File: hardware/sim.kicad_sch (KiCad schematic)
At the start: 11 parts, among them J12 Conn_01x06, J13 SIM_Card

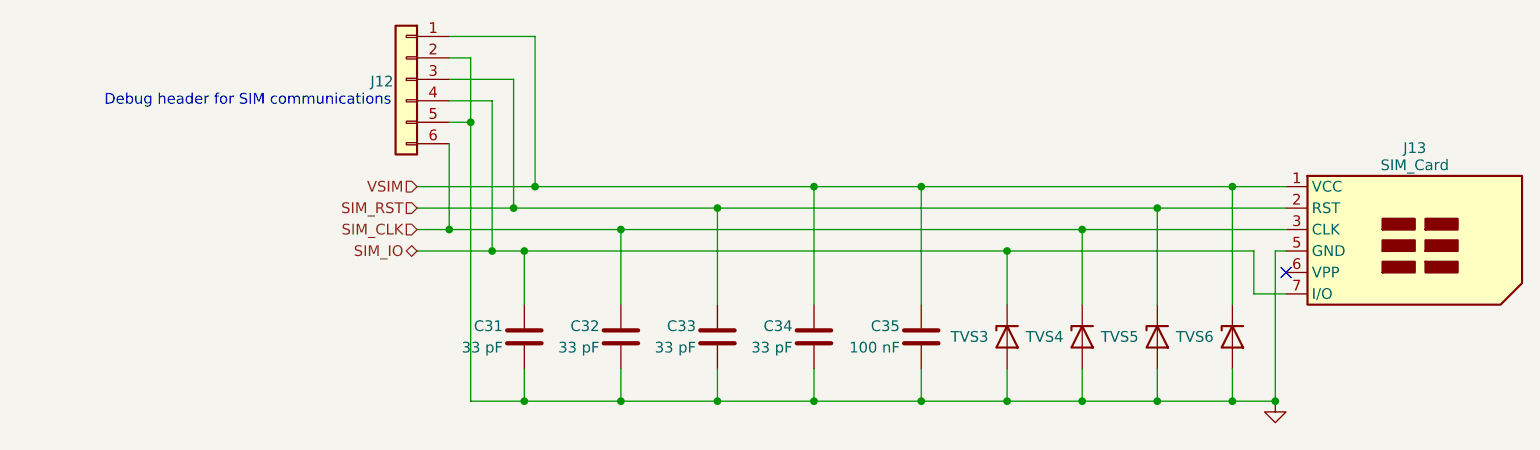
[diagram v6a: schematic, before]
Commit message: HW: Cleanup schematic
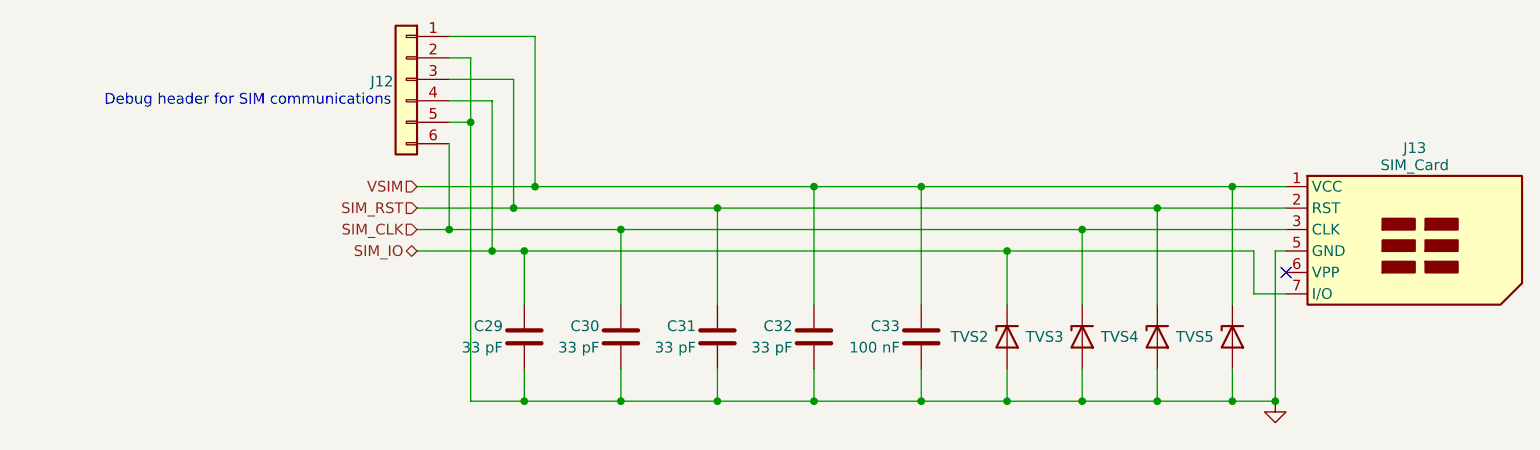
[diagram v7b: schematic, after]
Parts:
- renumbered C31 to C29, C32 to C30, C33 to C31, C34 to C32, C35 to C33, TVS3 to TVS2, TVS4 to TVS3, TVS5 to TVS4, TVS6 to TVS5
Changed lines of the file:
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@@
 		(on_board yes)
 		(dnp no)
-		(property "Reference" "C35"
+		(property "Reference" "C33"
 			(at 143.51 135.89 0)
 			(effects
@@
 			(project "iida_devkit"
 				(path "/b12a6e25-97fb-4aba-bc96-af8db389bb9a/33580d9f-a609-4568-baaf-9a29cf2dabcd"
-					(reference "C35")
+					(reference "C33")
 					(unit 1)
 				)
@@
 		(on_board yes)
 		(dnp no)
-		(property "Reference" "TVS4"
+		(property "Reference" "TVS3"
 			(at 160.655 137.16 90)
 			(effects
@@
 			(project "iida_devkit"
 				(path "/b12a6e25-97fb-4aba-bc96-af8db389bb9a/33580d9f-a609-4568-baaf-9a29cf2dabcd"
-					(reference "TVS4")
+					(reference "TVS3")
 					(unit 1)
 				)
@@
 		(on_board yes)
 		(dnp no)
-		(property "Reference" "C32"
+		(property "Reference" "C30"
 			(at 107.95 135.89 0)
 			(effects
@@
 			(project "iida_devkit"
 				(path "/b12a6e25-97fb-4aba-bc96-af8db389bb9a/33580d9f-a609-4568-baaf-9a29cf2dabcd"
-					(reference "C32")
+					(reference "C30")
 					(unit 1)
 				)
@@
 		(on_board yes)
 		(dnp no)
-		(property "Reference" "C31"
+		(property "Reference" "C29"
 			(at 96.52 135.89 0)
 			(effects
@@
 			(project "iida_devkit"
 				(path "/b12a6e25-97fb-4aba-bc96-af8db389bb9a/33580d9f-a609-4568-baaf-9a29cf2dabcd"
-					(reference "C31")
+					(reference "C29")
 					(unit 1)
 				)
@@
 		(on_board yes)
 		(dnp no)
-		(property "Reference" "TVS6"
+		(property "Reference" "TVS5"
 			(at 178.435 137.16 90)
 			(effects
@@
 			(project "iida_devkit"
 				(path "/b12a6e25-97fb-4aba-bc96-af8db389bb9a/33580d9f-a609-4568-baaf-9a29cf2dabcd"
-					(reference "TVS6")
+					(reference "TVS5")
 					(unit 1)
 				)
@@
 		(on_board yes)
 		(dnp no)
-		(property "Reference" "TVS3"
+		(property "Reference" "TVS2"
 			(at 151.765 137.16 90)
 			(effects
@@
 			(project "iida_devkit"
 				(path "/b12a6e25-97fb-4aba-bc96-af8db389bb9a/33580d9f-a609-4568-baaf-9a29cf2dabcd"
-					(reference "TVS3")
+					(reference "TVS2")
 					(unit 1)
 				)
@@
 		(on_board yes)
 		(dnp no)
-		(property "Reference" "C33"
+		(property "Reference" "C31"
 			(at 119.38 135.89 0)
 			(effects
@@
 			(project "iida_devkit"
 				(path "/b12a6e25-97fb-4aba-bc96-af8db389bb9a/33580d9f-a609-4568-baaf-9a29cf2dabcd"
-					(reference "C33")
+					(reference "C31")
 					(unit 1)
 				)
@@
 		(on_board yes)
 		(dnp no)
-		(property "Reference" "TVS5"
+		(property "Reference" "TVS4"
 			(at 169.545 137.16 90)
 			(effects
@@
 			(project "iida_devkit"
 				(path "/b12a6e25-97fb-4aba-bc96-af8db389bb9a/33580d9f-a609-4568-baaf-9a29cf2dabcd"
-					(reference "TVS5")
+					(reference "TVS4")
 					(unit 1)
 				)
@@
 		(dnp no)
 		(fields_autoplaced yes)
-		(property "Reference" "#PWR026"
+		(property "Reference" "#PWR024"
 			(at 187.96 151.13 0)
 			(effects
@@
 			(project "iida_devkit"
 				(path "/b12a6e25-97fb-4aba-bc96-af8db389bb9a/33580d9f-a609-4568-baaf-9a29cf2dabcd"
-					(reference "#PWR026")
+					(reference "#PWR024")
 					(unit 1)
 				)
@@
 		(on_board yes)
 		(dnp no)
-		(property "Reference" "C34"
+		(property "Reference" "C32"
 			(at 130.81 135.89 0)
 			(effects
@@
 			(project "iida_devkit"
 				(path "/b12a6e25-97fb-4aba-bc96-af8db389bb9a/33580d9f-a609-4568-baaf-9a29cf2dabcd"
-					(reference "C34")
-					(unit 1)
-				)
+					(reference "C32")
+					(unit 1)
+				)

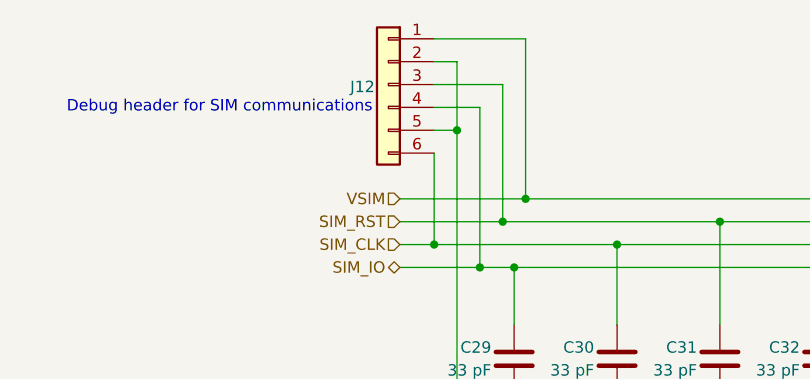
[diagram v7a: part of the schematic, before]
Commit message: HW: Route MCU
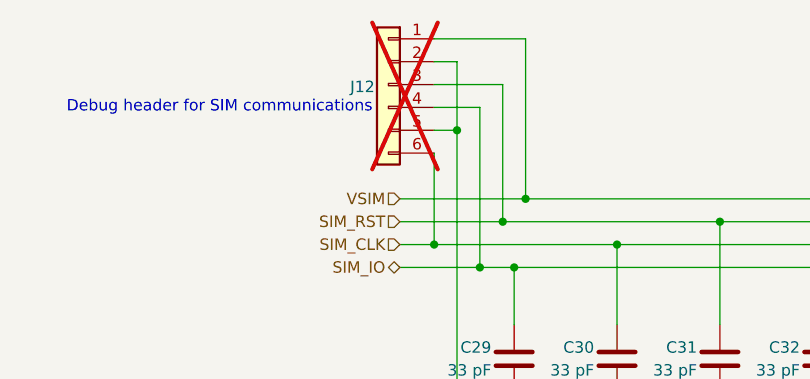
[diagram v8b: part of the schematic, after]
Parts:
- J12: now not fitted
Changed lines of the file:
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@@
 		(in_bom yes)
 		(on_board yes)
-		(dnp no)
+		(dnp yes)
 		(property "Reference" "J12"
 			(at 83.566 106.934 0)
